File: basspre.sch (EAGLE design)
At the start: 25 parts, among them U101 TLE2426IDR, U102 LF351D, U103 LM4250

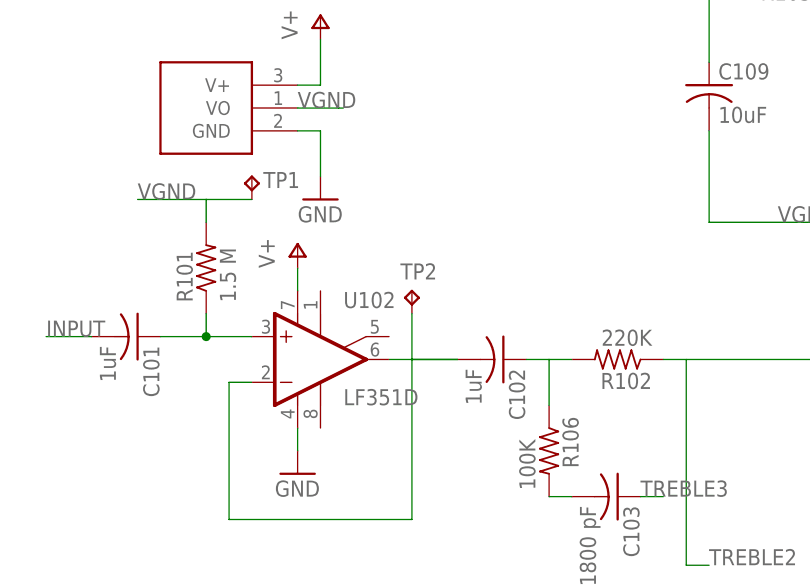
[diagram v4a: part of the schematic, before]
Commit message: switched to two lm4250s for micropower operation, added readme
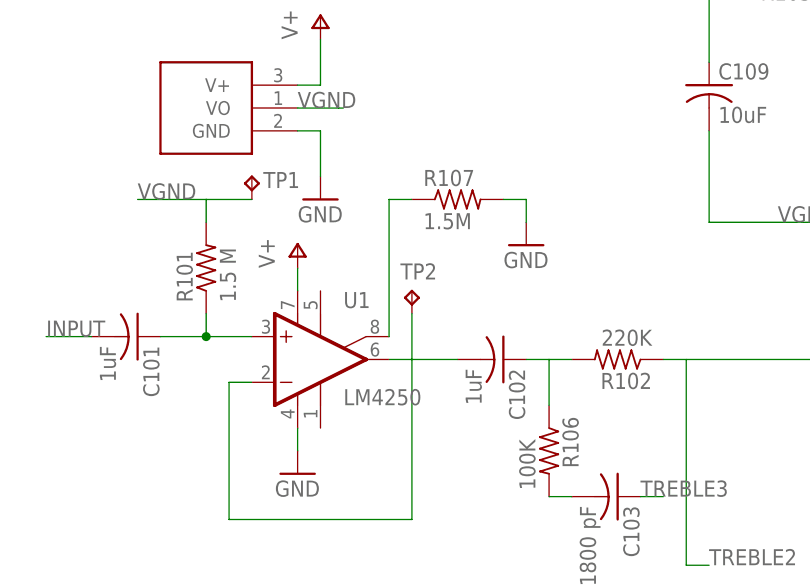
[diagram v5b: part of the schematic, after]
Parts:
- removed U102: LF351D, linear:LF351D
- added R107: 1.5M, resistor:R-US_R0603
- added U1: LM4250, russell_random:LM4250
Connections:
- new net R107: R107.1, U1.CURRENT
- net C1: now also U1.+IN; no longer U102.+IN
- net GND: now also R107.2, U1.V-; no longer U102.V-
- net N$3: now also U1.-IN, U1.OUT; no longer U102.-IN, U102.OUT
- net V+: now also U1.V+; no longer U102.V+
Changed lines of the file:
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@@
 <part name="R104" library="resistor" deviceset="R-US_" device="R0603" value="1.5M"/>
 <part name="GND3" library="supply1" deviceset="GND" device=""/>
-<part name="U102" library="linear" deviceset="LF351" device="D"/>
 <part name="GND4" library="supply1" deviceset="GND" device=""/>
 <part name="P+3" library="supply1" deviceset="V+" device=""/>
@@
 <part name="C109" library="resistor" deviceset="C-US" device="C0603" value="10uF"/>
 <part name="R106" library="resistor" deviceset="R-US_" device="R0603" value="100K"/>
+<part name="U1" library="russell_random" deviceset="LM4250" device=""/>
+<part name="R107" library="resistor" deviceset="R-US_" device="R0603" value="1.5M"/>
+<part name="GND7" library="supply1" deviceset="GND" device=""/>
 </parts>
 <sheets>
@@
 <instance part="R104" gate="G$1" x="137.16" y="149.86"/>
 <instance part="GND3" gate="1" x="147.32" y="139.7"/>
-<instance part="U102" gate="A" x="38.1" y="134.62"/>
 <instance part="GND4" gate="1" x="35.56" y="121.92"/>
 <instance part="P+3" gate="1" x="35.56" y="147.32"/>
@@
 <attribute name="VALUE" x="60.198" y="125.73" size="1.778" layer="96" rot="R270"/>
 </instance>
+<instance part="U1" gate="G$1" x="40.64" y="137.16"/>
+<instance part="R107" gate="G$1" x="53.34" y="152.4"/>
+<instance part="GND7" gate="1" x="60.96" y="147.32"/>
 </instances>
 <busses>
@@
 </segment>
 <segment>
-<pinref part="U102" gate="A" pin="V-"/>
 <pinref part="GND4" gate="1" pin="GND"/>
 <wire x1="35.56" y1="127" x2="35.56" y2="124.46" width="0.1524" layer="91"/>
+<pinref part="U1" gate="G$1" pin="V-"/>
 </segment>
 <segment>
@@
 <label x="185.42" y="152.4" size="1.778" layer="95"/>
 </segment>
+<segment>
+<pinref part="R107" gate="G$1" pin="2"/>
+<wire x1="58.42" y1="152.4" x2="60.96" y2="152.4" width="0.1524" layer="91"/>
+<pinref part="GND7" gate="1" pin="GND"/>
+<wire x1="60.96" y1="152.4" x2="60.96" y2="149.86" width="0.1524" layer="91"/>
+</segment>
 </net>
 <net name="V+" class="0">
@@
 </segment>
 <segment>
-<pinref part="U102" gate="A" pin="V+"/>
 <pinref part="P+3" gate="1" pin="V+"/>
 <wire x1="35.56" y1="144.78" x2="35.56" y2="142.24" width="0.1524" layer="91"/>
+<pinref part="U1" gate="G$1" pin="V+"/>
 </segment>
 <segment>
@@
 <wire x1="48.26" y1="116.84" x2="27.94" y2="116.84" width="0.1524" layer="91"/>
 <wire x1="27.94" y1="116.84" x2="27.94" y2="132.08" width="0.1524" layer="91"/>
-<pinref part="U102" gate="A" pin="-IN"/>
 <wire x1="27.94" y1="132.08" x2="30.48" y2="132.08" width="0.1524" layer="91"/>
 <wire x1="48.26" y1="116.84" x2="48.26" y2="134.62" width="0.1524" layer="91"/>
-<pinref part="U102" gate="A" pin="OUT"/>
 <wire x1="48.26" y1="134.62" x2="45.72" y2="134.62" width="0.1524" layer="91"/>
 <pinref part="C102" gate="G$1" pin="2"/>
-<wire x1="48.26" y1="134.62" x2="53.34" y2="134.62" width="0.1524" layer="91"/>
 <pinref part="TP2" gate="G$1" pin="TP"/>
 <wire x1="48.26" y1="134.62" x2="48.26" y2="139.7" width="0.1524" layer="91"/>
 <wire x1="48.26" y1="134.62" x2="53.34" y2="134.62" width="0.1524" layer="91"/>
+<pinref part="U1" gate="G$1" pin="-IN"/>
+<pinref part="U1" gate="G$1" pin="OUT"/>
 </segment>
 </net>
 <net name="C1" class="0">
 <segment>
-<pinref part="U102" gate="A" pin="+IN"/>
 <wire x1="30.48" y1="137.16" x2="25.4" y2="137.16" width="0.1524" layer="91"/>
 <pinref part="C101" gate="G$1" pin="1"/>
@@
 <wire x1="25.4" y1="137.16" x2="25.4" y2="139.7" width="0.1524" layer="91"/>
 <junction x="25.4" y="137.16"/>
+<pinref part="U1" gate="G$1" pin="+IN"/>
 </segment>
 </net>
@@
 </segment>
 </net>
+<net name="R107" class="0">
+<segment>
+<pinref part="U1" gate="G$1" pin="CURRENT"/>
+<wire x1="45.72" y1="137.16" x2="45.72" y2="152.4" width="0.1524" layer="91"/>
+<pinref part="R107" gate="G$1" pin="1"/>
+<wire x1="45.72" y1="152.4" x2="48.26" y2="152.4" width="0.1524" layer="91"/>
+</segment>
+</net>

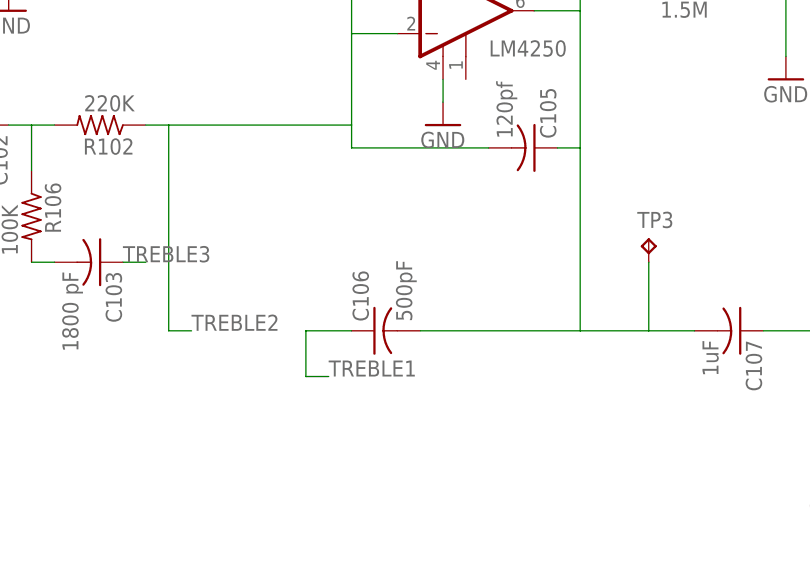
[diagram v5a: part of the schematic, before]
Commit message: changed bypass caps to 0805.
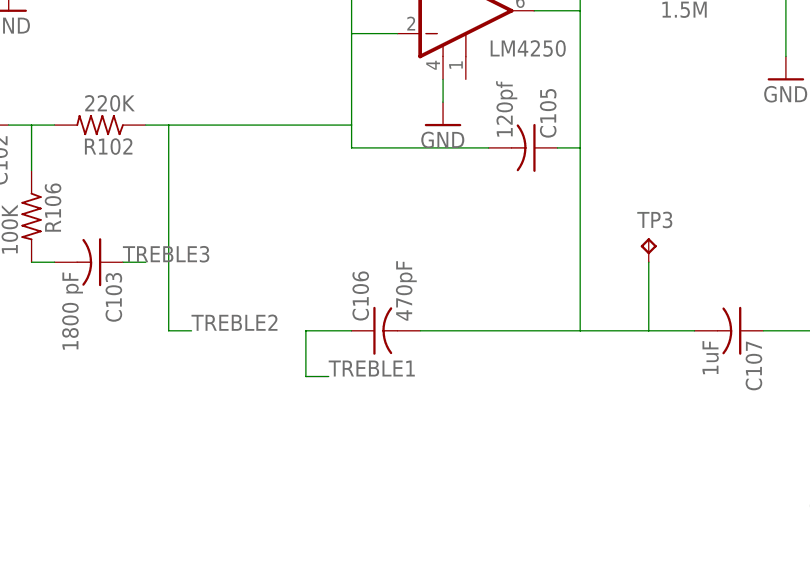
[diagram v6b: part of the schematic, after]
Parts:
- C101, C102, C107: device resistor:C-USC0603 -> rcl:C-USC0805
- C106: value 500pF -> 470pF
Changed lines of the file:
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@@
 <part name="GND4" library="supply1" deviceset="GND" device=""/>
 <part name="P+3" library="supply1" deviceset="V+" device=""/>
-<part name="C101" library="resistor" deviceset="C-US" device="C0603" value="1uF"/>
+<part name="C101" library="rcl" deviceset="C-US" device="C0805" value="1uF"/>
 <part name="R101" library="resistor" deviceset="R-US_" device="R0603" value="1.5 M"/>
 <part name="C105" library="resistor" deviceset="C-US" device="C0603" value="120pf"/>
 <part name="R103" library="resistor" deviceset="R-US_" device="R0603" value="100K"/>
 <part name="C108" library="resistor" deviceset="C-US" device="C0603" value="47nF"/>
-<part name="C102" library="resistor" deviceset="C-US" device="C0603" value="1uF"/>
+<part name="C102" library="rcl" deviceset="C-US" device="C0805" value="1uF"/>
 <part name="R102" library="resistor" deviceset="R-US_" device="R0603" value="220K"/>
 <part name="C103" library="resistor" deviceset="C-US" device="C0603" value="1800 pF"/>
-<part name="C106" library="resistor" deviceset="C-US" device="C0603" value="500pF"/>
-<part name="C107" library="resistor" deviceset="C-US" device="C0603" value="1uF"/>
+<part name="C106" library="resistor" deviceset="C-US" device="C0603" value="470pF"/>
+<part name="C107" library="rcl" deviceset="C-US" device="C0805" value="1uF"/>
 <part name="GND5" library="supply1" deviceset="GND" device=""/>
 <part name="TP1" library="testpad" deviceset="TP" device="PAD1-13"/>

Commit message: added mouser order
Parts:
- C109: device resistor:C-USC0603 -> rcl:C-USC0805
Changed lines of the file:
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@@
 <part name="GND6" library="supply1" deviceset="GND" device=""/>
 <part name="R105" library="resistor" deviceset="R-US_" device="R0603" value="10K"/>
-<part name="C109" library="resistor" deviceset="C-US" device="C0603" value="10uF"/>
+<part name="C109" library="rcl" deviceset="C-US" device="C0805" value="10uF"/>
 <part name="R106" library="resistor" deviceset="R-US_" device="R0603" value="100K"/>
 <part name="U1" library="russell_random" deviceset="LM4250" device=""/>
